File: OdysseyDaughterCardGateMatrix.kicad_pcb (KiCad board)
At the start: 2 copper layers, 35 x 46.6 mm, 17 parts, among them X1 OdysseyDaughterCard

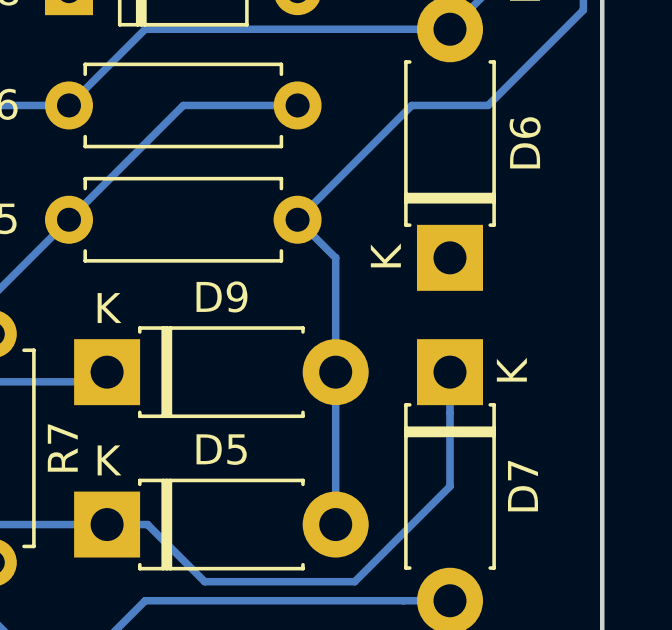
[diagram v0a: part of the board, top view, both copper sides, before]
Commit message: Add forgotten trace
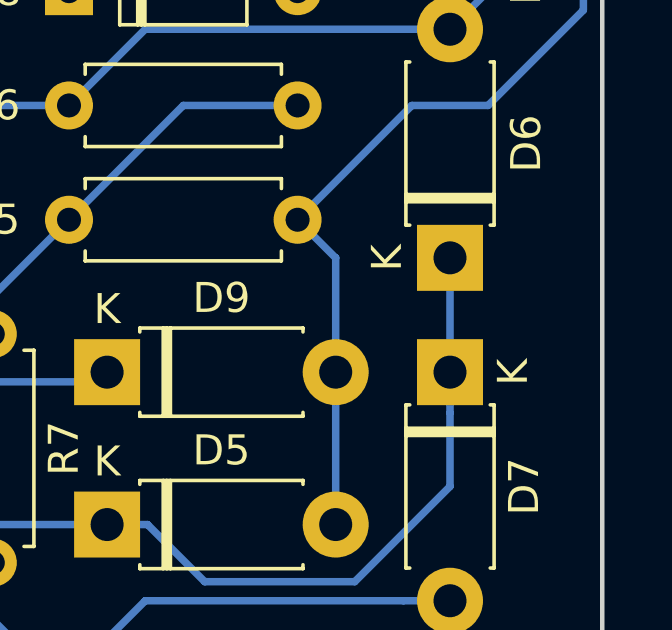
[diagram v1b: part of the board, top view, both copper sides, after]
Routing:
- net /Card4: track 29.5 -> 33.3 mm
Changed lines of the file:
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@@
     (thickness 1.6)
     (drawings 13)
-    (tracks 69)
+    (tracks 70)
     (zones 0)
     (modules 17)
@@
   (segment (start 147.32 80.01) (end 148.745001 78.584999) (width 0.25) (layer B.Cu) (net 6))
   (segment (start 148.745001 78.584999) (end 153.514999 78.584999) (width 0.25) (layer B.Cu) (net 6))
+  (segment (start 152.4 102.87) (end 152.4 99.06) (width 0.25) (layer B.Cu) (net 7))
   (segment (start 142.32 107.95) (end 144.225 109.855) (width 0.25) (layer B.Cu) (net 7))
   (segment (start 140.97 107.95) (end 142.32 107.95) (width 0.25) (layer B.Cu) (net 7))

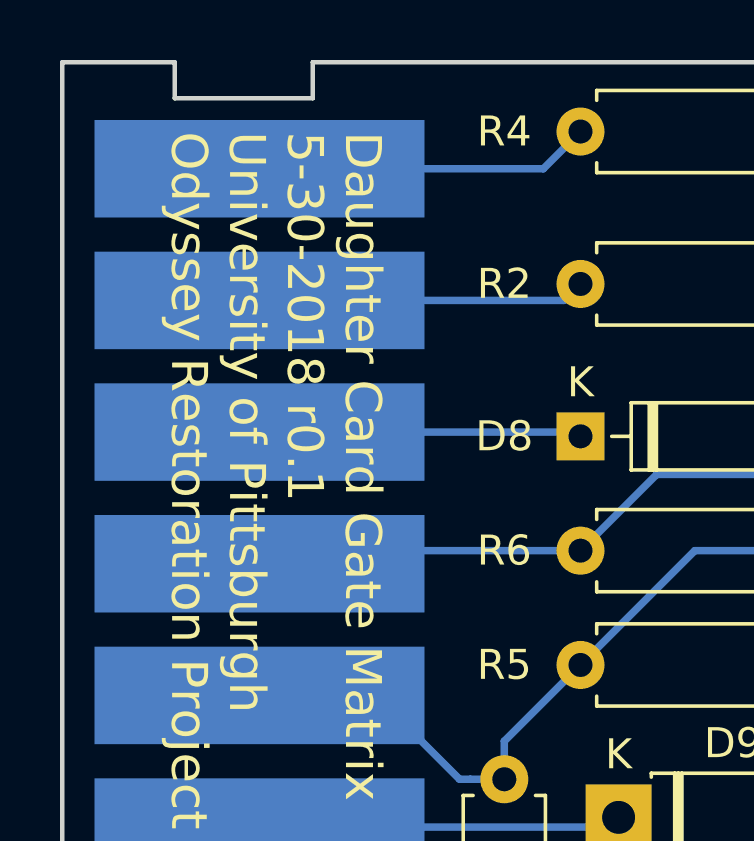
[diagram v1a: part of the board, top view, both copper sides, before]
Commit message: Change diode types, bump rev #
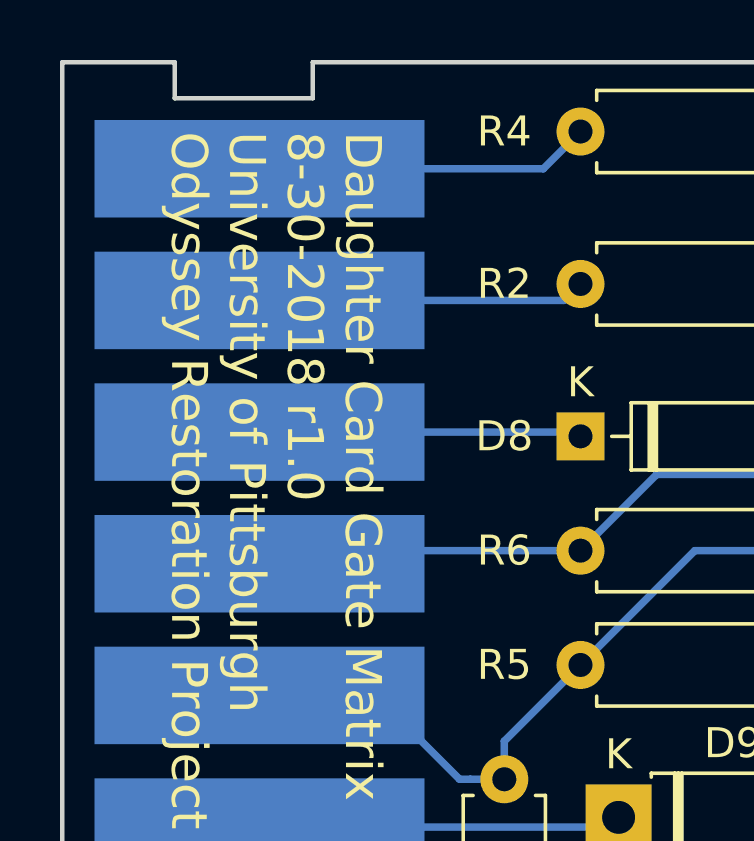
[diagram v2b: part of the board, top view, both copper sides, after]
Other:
- board text added: "Daughter Card Gate Matrix 8-30-2018 r1.0 University of Pittsburgh Odyssey Restoration Project"
- board text removed: "Daughter Card Gate Matrix 5-30-2018 r0.1 University of Pittsburgh Odyssey Restoration Project"
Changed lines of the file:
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@@
   (title_block
     (title "Odyssey Daughter Card Template")
-    (date 2018-05-29)
-    (rev 0.1)
+    (date 2018-08-30)
+    (rev 1.0)
     (company "University of Pittsburgh - Odyssey Restoration Project")
     (comment 1 "Levi Burner")
@@
   (gr_line (start 126.175 124.3) (end 126.175 123.1) (layer Edge.Cuts) (width 0.15))
   (gr_line (start 122.425 124.3) (end 126.175 124.3) (layer Edge.Cuts) (width 0.15))
-  (gr_text "Daughter Card Gate Matrix\n5-30-2018 r0.1\nUniversity of Pittsburgh\nOdyssey Restoration Project" (at 129.54 80.01 -90) (layer F.SilkS)
+  (gr_text "Daughter Card Gate Matrix\n8-30-2018 r1.0\nUniversity of Pittsburgh\nOdyssey Restoration Project" (at 129.54 80.01 -90) (layer F.SilkS)
     (effects (font (size 1.2 1.2) (thickness 0.2)) (justify left))
   )

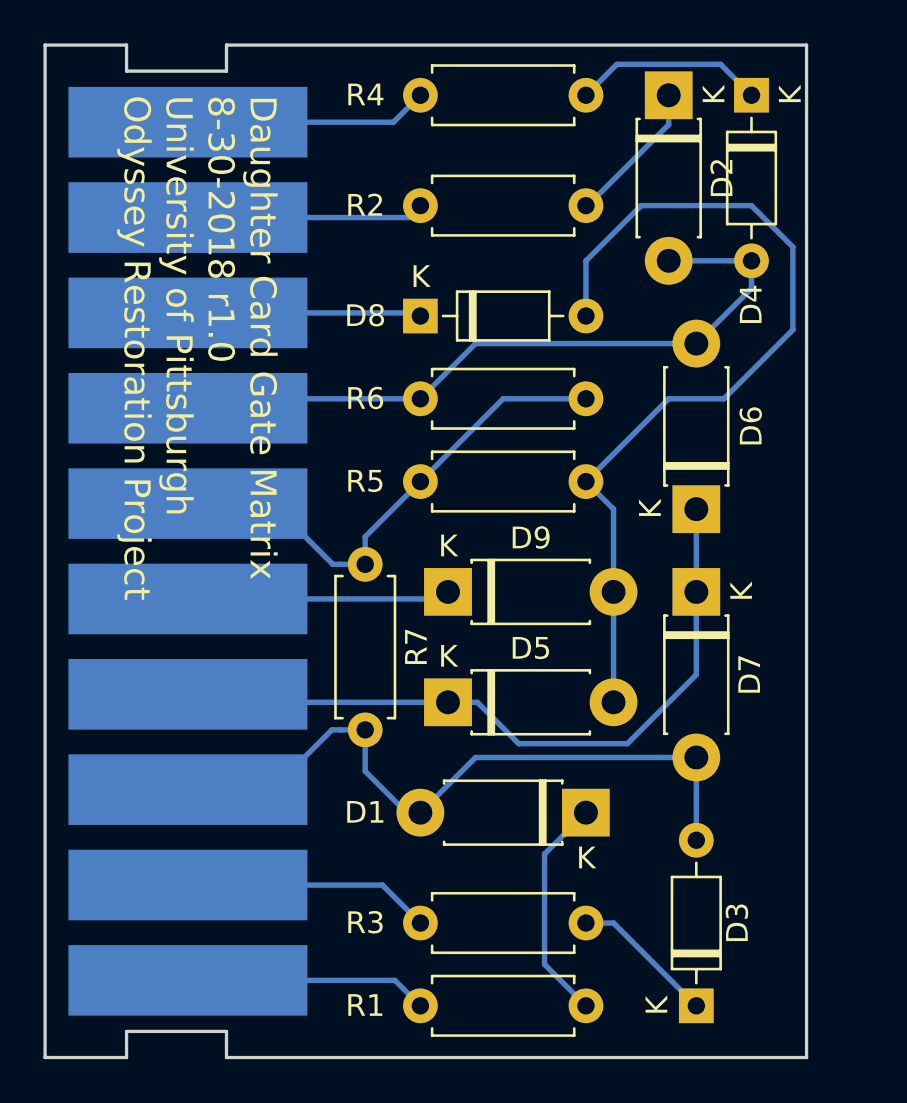
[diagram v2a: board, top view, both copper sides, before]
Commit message: R1.0 Add header for extra player generator
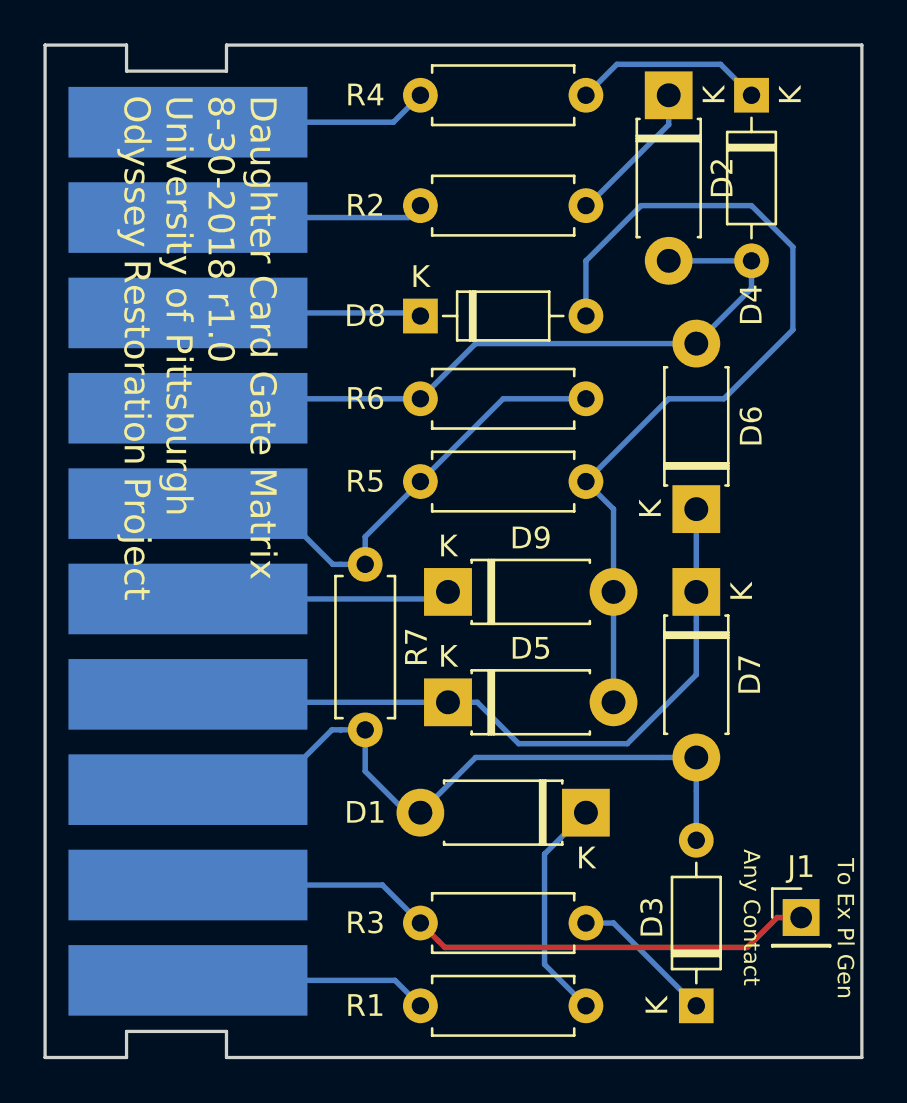
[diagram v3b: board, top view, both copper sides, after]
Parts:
- added J1: Conn_01x01, Connector_PinHeader_2.54mm:PinHeader_1x01_P2.54mm_Vertical, F.Cu at (157.2, 117.9)
- D1, D2, D5, D6, D7, D9: value 11DQ04TR -> BAT83S
- D3, D4, D8: value 1N4148 -> 1N4448
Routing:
- net /Card2: track 11.4 -> 30.0 mm
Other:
- board size 35 x 46.6 mm -> 37.6 x 46.6 mm
- board text added: "Any Contact"
- board text added: "To Ex Pl Gen"
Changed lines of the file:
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@@
-(kicad_pcb (version 20171130) (host pcbnew "(2017-12-21 revision 23d71cfa9)-makepkg")
+(kicad_pcb (version 20171130) (host pcbnew "(5.0.1)-3")
   (general
     (thickness 1.6)
-    (drawings 13)
-    (tracks 70)
+    (drawings 15)
+    (tracks 75)
     (zones 0)
-    (modules 17)
+    (modules 18)
     (nets 16)
   )
@@
     (pad_drill 0.762)
     (pad_to_mask_clearance 0.2)
+    (solder_mask_min_width 0.25)
     (aux_axis_origin 0 0)
     (visible_elements 7FFFFFFF)
     (pcbplotparams
       (layerselection 0x010f0_ffffffff)
-      (usegerberextensions true)
+      (usegerberextensions false)
       (usegerberattributes false)
       (usegerberadvancedattributes false)
@@
       (hpglpennumber 1)
       (hpglpenspeed 20)
-      (hpglpendiameter 15)
+      (hpglpendiameter 15.000000)
       (psnegative false)
       (psa4output false)
@@
       (drillshape 0)
       (scaleselection 1)
-      (outputdirectory gerbers/))
+      (outputdirectory "gerbers/"))
   )
   (net 0 "")
@@
       (effects (font (size 1 1) (thickness 0.15)))
     )
-    (fp_text value 11DQ04TR (at 3.81 2.47 180) (layer F.Fab)
+    (fp_text value BAT83S (at 3.81 2.47 180) (layer F.Fab)
       (effects (font (size 1 1) (thickness 0.15)))
     )
@@
       (effects (font (size 1 1) (thickness 0.15)))
     )
-    (fp_text value 11DQ04TR (at 3.81 2.47 270) (layer F.Fab)
+    (fp_text value BAT83S (at 3.81 2.47 270) (layer F.Fab)
       (effects (font (size 1 1) (thickness 0.15)))
     )
@@
     (descr "D, DO-35_SOD27 series, Axial, Horizontal, pin pitch=7.62mm, , length*diameter=4*2mm^2, , http://www.diodes.com/_files/packages/DO-35.pdf")
     (tags "D DO-35_SOD27 series Axial Horizontal pin pitch 7.62mm  length 4mm diameter 2mm")
-    (fp_text reference D3 (at 3.81 1.905 90) (layer F.SilkS)
-      (effects (font (size 1 1) (thickness 0.15)))
-    )
-    (fp_text value 1N4148 (at 3.81 2.12 90) (layer F.Fab)
+    (fp_text reference D3 (at 4.064 -2.032 90) (layer F.SilkS)
+      (effects (font (size 1 1) (thickness 0.15)))
+    )
+    (fp_text value 1N4448 (at 3.81 2.12 90) (layer F.Fab)
       (effects (font (size 1 1) (thickness 0.15)))
     )
@@
       (effects (font (size 1 1) (thickness 0.15)))
     )
-    (fp_text value 1N4148 (at 3.81 2.12 270) (layer F.Fab)
+    (fp_text value 1N4448 (at 3.81 2.12 270) (layer F.Fab)
       (effects (font (size 1 1) (thickness 0.15)))
     )
@@
       (effects (font (size 1 1) (thickness 0.15)))
     )
-    (fp_text value 11DQ04TR (at 3.81 2.47) (layer F.Fab)
+    (fp_text value BAT83S (at 3.81 2.47) (layer F.Fab)
       (effects (font (size 1 1) (thickness 0.15)))
     )
@@
       (effects (font (size 1 1) (thickness 0.15)))
     )
-    (fp_text value 11DQ04TR (at 3.81 2.47 90) (layer F.Fab)
+    (fp_text value BAT83S (at 3.81 2.47 90) (layer F.Fab)
       (effects (font (size 1 1) (thickness 0.15)))
     )
@@
       (effects (font (size 1 1) (thickness 0.15)))
     )
-    (fp_text value 11DQ04TR (at 3.81 2.47 270) (layer F.Fab)
+    (fp_text value BAT83S (at 3.81 2.47 270) (layer F.Fab)
       (effects (font (size 1 1) (thickness 0.15)))
     )
@@
       (effects (font (size 1 1) (thickness 0.15)))
     )
-    (fp_text value 1N4148 (at 3.81 2.12) (layer F.Fab)
+    (fp_text value 1N4448 (at 3.81 2.12) (layer F.Fab)
       (effects (font (size 1 1) (thickness 0.15)))
     )
@@
       (effects (font (size 1 1) (thickness 0.15)))
     )
-    (fp_text value 11DQ04TR (at 3.81 2.47) (layer F.Fab)
+    (fp_text value BAT83S (at 3.81 2.47) (layer F.Fab)
       (effects (font (size 1 1) (thickness 0.15)))
     )
@@
     )
   )
-  (gr_line (start 157.475 77.7) (end 157.475 124.3) (layer Edge.Cuts) (width 0.15))
+  (module Connector_PinHeader_2.54mm:PinHeader_1x01_P2.54mm_Vertical (layer F.Cu)
+    (at 157.226 117.856)
+    (descr "Through hole straight pin header, 1x01, 2.54mm pitch, single row")
+    (tags "Through hole pin header THT 1x01 2.54mm single row")
+    (fp_text reference J1 (at 0 -2.33) (layer F.SilkS)
+      (effects (font (size 1 1) (thickness 0.15)))
+    )
+    (fp_text value Conn_01x01 (at 0 2.33) (layer F.Fab)
+      (effects (font (size 1 1) (thickness 0.15)))
+    )
+    (fp_line (start -0.635 -1.27) (end 1.27 -1.27) (layer F.Fab) (width 0.1))
+    (fp_line (start 1.27 -1.27) (end 1.27 1.27) (layer F.Fab) (width 0.1))
+    (fp_line (start 1.27 1.27) (end -1.27 1.27) (layer F.Fab) (width 0.1))
+    (fp_line (start -1.27 1.27) (end -1.27 -0.635) (layer F.Fab) (width 0.1))
+    (fp_line (start -1.27 -0.635) (end -0.635 -1.27) (layer F.Fab) (width 0.1))
+    (fp_line (start -1.33 1.33) (end 1.33 1.33) (layer F.SilkS) (width 0.12))
+    (fp_line (start -1.33 1.27) (end -1.33 1.33) (layer F.SilkS) (width 0.12))
+    (fp_line (start 1.33 1.27) (end 1.33 1.33) (layer F.SilkS) (width 0.12))
+    (fp_line (start -1.33 1.27) (end 1.33 1.27) (layer F.SilkS) (width 0.12))
+    (fp_line (start -1.33 0) (end -1.33 -1.33) (layer F.SilkS) (width 0.12))
+    (fp_line (start -1.33 -1.33) (end 0 -1.33) (layer F.SilkS) (width 0.12))
+    (fp_line (start -1.8 -1.8) (end -1.8 1.8) (layer F.CrtYd) (width 0.05))
+    (fp_line (start -1.8 1.8) (end 1.8 1.8) (layer F.CrtYd) (width 0.05))
+    (fp_line (start 1.8 1.8) (end 1.8 -1.8) (layer F.CrtYd) (width 0.05))
+    (fp_line (start 1.8 -1.8) (end -1.8 -1.8) (layer F.CrtYd) (width 0.05))
+    (fp_text user %R (at 0 0 90) (layer F.Fab)
+      (effects (font (size 1 1) (thickness 0.15)))
+    )
+    (pad 1 thru_hole rect (at 0 0) (size 1.7 1.7) (drill 1) (layers *.Cu *.Mask)
+      (net 13 /Card2))
+    (model ${KISYS3DMOD}/Connector_PinHeader_2.54mm.3dshapes/PinHeader_1x01_P2.54mm_Vertical.wrl
+      (at (xyz 0 0 0))
+      (scale (xyz 1 1 1))
+      (rotate (xyz 0 0 0))
+    )
+  )
+  (gr_text "Any Contact" (at 154.94 117.856 270) (layer F.SilkS)
+    (effects (font (size 0.75 0.75) (thickness 0.1)))
+  )
+  (gr_text "To Ex Pl Gen" (at 159.258 118.364 270) (layer F.SilkS)
+    (effects (font (size 0.75 0.75) (thickness 0.1)))
+  )
+  (gr_line (start 160.02 77.7) (end 160.02 124.3) (layer Edge.Cuts) (width 0.15))
   (gr_line (start 126.175 77.7) (end 122.425 77.7) (layer Edge.Cuts) (width 0.15))
   (gr_line (start 126.175 78.9) (end 126.175 77.7) (layer Edge.Cuts) (width 0.15))
   (gr_line (start 130.775 78.9) (end 126.175 78.9) (layer Edge.Cuts) (width 0.15))
   (gr_line (start 130.775 77.7) (end 130.775 78.9) (layer Edge.Cuts) (width 0.15))
-  (gr_line (start 157.475 77.7) (end 130.775 77.7) (layer Edge.Cuts) (width 0.15))
-  (gr_line (start 130.775 124.3) (end 157.475 124.3) (layer Edge.Cuts) (width 0.15))
+  (gr_line (start 160.02 77.7) (end 130.775 77.7) (layer Edge.Cuts) (width 0.15))
+  (gr_line (start 130.775 124.3) (end 160.02 124.3) (layer Edge.Cuts) (width 0.15))
   (gr_line (start 130.775 123.1) (end 130.775 124.3) (layer Edge.Cuts) (width 0.15))
   (gr_line (start 126.175 123.1) (end 130.775 123.1) (layer Edge.Cuts) (width 0.15))
@@
   (segment (start 129 116.361104) (end 137.951104 116.361104) (width 0.25) (layer B.Cu) (net 13))
   (segment (start 137.951104 116.361104) (end 139.7 118.11) (width 0.25) (layer B.Cu) (net 13))
+  (segment (start 140.499999 118.909999) (end 139.7 118.11) (width 0.25) (layer F.Cu) (net 13))
+  (segment (start 140.825001 119.235001) (end 140.499999 118.909999) (width 0.25) (layer F.Cu) (net 13))
+  (segment (start 154.746999 119.235001) (end 140.825001 119.235001) (width 0.25) (layer F.Cu) (net 13))
+  (segment (start 156.126 117.856) (end 154.746999 119.235001) (width 0.25) (layer F.Cu) (net 13))
+  (segment (start 157.226 117.856) (end 156.126 117.856) (width 0.25) (layer F.Cu) (net 13))
   (segment (start 129 81.25) (end 138.46 81.25) (width 0.25) (layer B.Cu) (net 14))
   (segment (start 138.46 81.25) (end 139.7 80.01) (width 0.25) (layer B.Cu) (net 14))
